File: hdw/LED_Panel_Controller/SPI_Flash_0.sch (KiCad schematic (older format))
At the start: 14 parts

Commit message: lots of schematic progress
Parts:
- removed U?: 74LVC1G07, TO_SOT_Packages_SMD:SOT-353_SC-70-5, symbol Custom_Library:74LVC1G07_Power
- added U?: 74LVC1G97, Package_TO_SOT_SMD:SOT-363_SC-70-6, symbol Custom_Library:74LVC1G97_Power_BUF
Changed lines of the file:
@@
 encoding utf-8
 Sheet 23 34
-Title "Electronic Display Logic Board"
-Date "2018-12-15"
+Title "LED Panel Controller"
+Date "2020-12-23"
 Rev "A"
-Comp "Marquette University Senior Design 2018/2019 Group E44"
+Comp "Drew Maatman, Logan Wedel"
 Comment1 ""
 Comment2 ""
@@
 F 7 "311-1344-1-ND" H 2435 7400 60  0001 C CNN "Digi-Key PN"
 	1    2010 6900
-	1    0    0    -1
-$EndComp
-$Comp
-L Custom_Library:74LVC1G07_Power U?
-U 1 1 5C161AE1
-P 1670 6320
-F 0 "U?" H 1770 6420 50  0000 L CNN
-F 1 "74LVC1G07" H 1770 6220 50  0000 L CNN
-F 2 "TO_SOT_Packages_SMD:SOT-353_SC-70-5" H 1670 6320 50  0001 C CNN
-F 3 "http://www.ti.com/lit/sg/scyt129e/scyt129e.pdf" H 1670 6320 50  0001 C CNN
-F 4 "296-8486-1-ND" H 1670 6320 50  0001 C CNN "Digi-Key PN"
-	1    1670 6320
 	1    0    0    -1
 $EndComp
@@
 	0    -1   1    0
 $EndComp
+$Comp
+L Custom_Library:74LVC1G97_Power_BUF U?
+U 1 1 5FE9D8D5
+P 1670 6320
+F 0 "U?" H 1730 6470 50  0000 L CNN
+F 1 "74LVC1G97" H 1730 6170 50  0000 L CNN
+F 2 "Package_TO_SOT_SMD:SOT-363_SC-70-6" H 1720 6320 50  0001 C CNN
+F 3 "http://www.ti.com/lit/ds/symlink/sn74lvc1g97.pdf" H 1720 6320 50  0001 C CNN
+	1    1670 6320
+	1    0    0    -1
+$EndComp
 $EndSCHEMATC

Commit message: made a lot more schematic progress
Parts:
- removed C?: 0.1uF, Capacitors_SMD:C_0603, symbol Custom_Library:C_Custom
- removed R? (x2): 10k, Resistors_SMD:R_0603, symbol Custom_Library:R_Custom
- removed R?: 1k, Resistors_SMD:R_0603, symbol Custom_Library:R_Custom
- added C?: 0.1uF, Capacitors_SMD:C_0603, symbol Custom_Library:C_Custom
- added R? (x2): 10k, Resistors_SMD:R_0603, symbol Custom_Library:R_Custom
- added R?: 1k, Resistors_SMD:R_0603, symbol Custom_Library:R_Custom
- C?, D?, R? (x4), U? (x2): Configuration (none) -> SPI_FLASH
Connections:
- net +3V3: now also C?.1, R?.1, R?.1
- net GND: now also C?.2, R?.2
- net at R?.1, U?.5 (SI): now also R?.1
- net at R?.1, U?.1 (~CE): now also R?.2
- net at D?.2 (A): now also R?.2
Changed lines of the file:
@@
-$Comp
-L Custom_Library:R_Custom R?
-U 1 1 5BB4E3FC
-P 5150 3930
-F 0 "R?" H 5090 3930 50  0000 R CNN
-F 1 "10k" V 5150 3930 50  0000 C CNN
-F 2 "Resistors_SMD:R_0603" H 5150 3930 50  0001 C CNN
-F 3 "" H 5150 3930 50  0001 C CNN
-F 4 "0603" H 5230 4010 50  0000 L CNN "display_footprint"
-F 5 "1%" H 5230 3930 50  0000 L CNN "Tolerance"
-F 6 "1/10W" H 5230 3850 50  0000 L CNN "Wattage"
-F 7 "RMCF0603FT10K0CT-ND" H 5450 4330 60  0001 C CNN "Digi-Key PN"
-	1    5150 3930
-	1    0    0    -1
-$EndComp
-$Comp
-L Custom_Library:R_Custom R?
-U 1 1 5BB4EBA3
-P 3930 3130
-F 0 "R?" H 3870 3130 50  0000 R CNN
-F 1 "10k" V 3930 3130 50  0000 C CNN
-F 2 "Resistors_SMD:R_0603" H 3930 3130 50  0001 C CNN
-F 3 "" H 3930 3130 50  0001 C CNN
-F 4 "0603" H 4010 3210 50  0000 L CNN "display_footprint"
-F 5 "1%" H 4010 3130 50  0000 L CNN "Tolerance"
-F 6 "1/10W" H 4010 3050 50  0000 L CNN "Wattage"
-F 7 "RMCF0603FT10K0CT-ND" H 4230 3530 60  0001 C CNN "Digi-Key PN"
-	1    3930 3130
-	1    0    0    -1
-$EndComp
 $Comp
 L Custom_Library:R_Custom R?
@@
 F 5 "1%" V 3620 3450 50  0001 C CNN "Tolerance"
 F 6 "1/16W" V 3720 3450 50  0001 C CNN "Wattage"
+F 7 "SPI_FLASH" V 3270 3450 50  0000 C CNN "Configuration"
 	1    3420 3450
 	0    1    1    0
@@
 F 6 "X7R" H 1860 6800 50  0000 R CNN "Dielectric"
 F 7 "311-1344-1-ND" H 2435 7400 60  0001 C CNN "Digi-Key PN"
+F 8 "SPI_FLASH" H 2340 6900 50  0000 C CNN "Configuration"
 	1    2010 6900
 	1    0    0    -1
@@
 	2410 6320 2410 6160
 $Comp
-L Custom_Library:R_Custom R?
-U 1 1 5C166A8D
-P 2410 5710
-AR Path="/5BAAE1F3/5C166A8D" Ref="R?"  Part="1"
-AR Path="/5BAAE1DC/5C166A8D" Ref="R?"  Part="1"
-AR Path="/5BAAE16C/5C166A8D" Ref="R?"  Part="1"
-AR Path="/5BB844FD/5C166A8D" Ref="R?"  Part="1"
-AR Path="/5BF346B3/5C166A8D" Ref="R?"  Part="1"
-AR Path="/5BB2595E/5C166A8D" Ref="R?"  Part="1"
-AR Path="/5F583577/5C166A8D" Ref="R?"  Part="1"
-F 0 "R?" H 2350 5710 50  0000 R CNN
-F 1 "1k" V 2410 5710 50  0000 C CNN
-F 2 "Resistors_SMD:R_0603" H 2410 5710 50  0001 C CNN
-F 3 "" H 2410 5710 50  0001 C CNN
-F 4 "0603" H 2480 5790 50  0000 L CNN "display_footprint"
-F 5 "1%" H 2480 5710 50  0000 L CNN "Tolerance"
-F 6 "1/10W" H 2480 5640 50  0000 L CNN "Wattage"
-F 7 "RMCF0603FT1K00CT-ND" H 2710 6110 60  0001 C CNN "Digi-Key PN"
-	1    2410 5710
-	-1   0    0    -1
-$EndComp
-$Comp
 L Device:LED D?
 U 1 1 5C166A95
@@
 AR Path="/5BB2595E/5C166A95" Ref="D?"  Part="1"
 AR Path="/5F583577/5C166A95" Ref="D?"  Part="1"
-F 0 "D?" V 2440 5890 50  0000 R CNN
-F 1 "Green" V 2357 5893 50  0000 R CNN
+F 0 "D?" V 2520 6120 50  0000 L CNN
+F 1 "Green" V 2420 6120 50  0000 L CNN
 F 2 "LEDs:LED_0603" H 2410 6010 50  0001 C CNN
 F 3 "~" H 2410 6010 50  0001 C CNN
 F 4 "160-1446-1-ND" H -2600 3010 50  0001 C CNN "Digi-Key PN"
+F 5 "SPI_FLASH" V 2320 6120 50  0000 L CNN "Configuration"
 	1    2410 6010
 	0    -1   -1   0
@@
 F 3 "http://ww1.microchip.com/downloads/en/DeviceDoc/20005045C.pdf" H 6030 4200 50  0001 C CNN
 F 4 "SST25VF080B-50-4I-S2AF-TCT-ND" H 6080 3650 50  0001 C CNN "Digi-Key PN"
+F 5 "SPI_FLASH" H 6080 3020 50  0000 C CNN "Configuration"
 	1    6080 3650
-	1    0    0    -1
-$EndComp
-$Comp
-L Custom_Library:C_Custom C?
-U 1 1 5F68928C
-P 6210 4700
-AR Path="/5BAAE16C/5F68928C" Ref="C?"  Part="1"
-AR Path="/5BB181D8/5F68928C" Ref="C?"  Part="1"
-AR Path="/5BB2595E/5F68928C" Ref="C?"  Part="1"
-AR Path="/5F583577/5F68928C" Ref="C?"  Part="1"
-F 0 "C?" H 6235 4800 50  0000 L CNN
-F 1 "0.1uF" H 6235 4600 50  0000 L CNN
-F 2 "Capacitors_SMD:C_0603" H 6248 4550 50  0001 C CNN
-F 3 "" H 6235 4800 50  0001 C CNN
-F 4 "0603" H 6060 4800 50  0000 R CNN "display_footprint"
-F 5 "50V" H 6060 4700 50  0000 R CNN "Voltage"
-F 6 "X7R" H 6060 4600 50  0000 R CNN "Dielectric"
-F 7 "311-1344-1-ND" H 6635 5200 60  0001 C CNN "Digi-Key PN"
-	1    6210 4700
 	1    0    0    -1
 $EndComp
@@
 F 6 "1/10W" H 4580 3850 50  0000 L CNN "Wattage"
 F 7 "RMCF0603FT10K0CT-ND" H 4800 4330 60  0001 C CNN "Digi-Key PN"
+F 8 "SPI_FLASH" H 4580 3770 50  0000 L CNN "Configuration"
 	1    4500 3930
 	1    0    0    -1
@@
 F 5 "1%" V 3620 3550 50  0001 C CNN "Tolerance"
 F 6 "1/16W" V 3720 3550 50  0001 C CNN "Wattage"
+F 7 "SPI_FLASH" H 3420 3550 50  0001 C CNN "Configuration"
 	1    3420 3550
 	0    1    1    0
@@
 F 5 "1%" V 3620 3650 50  0001 C CNN "Tolerance"
 F 6 "1/16W" V 3720 3650 50  0001 C CNN "Wattage"
+F 7 "SPI_FLASH" H 3420 3650 50  0001 C CNN "Configuration"
 	1    3420 3650
 	0    1    1    0
@@
 F 2 "Package_TO_SOT_SMD:SOT-363_SC-70-6" H 1720 6320 50  0001 C CNN
 F 3 "http://www.ti.com/lit/ds/symlink/sn74lvc1g97.pdf" H 1720 6320 50  0001 C CNN
+F 4 "SPI_FLASH" H 1370 6470 50  0000 C CNN "Configuration"
 	1    1670 6320
 	1    0    0    -1
 $EndComp
+$Comp
+L Custom_Library:R_Custom R?
+U 1 1 6026393A
+P 5150 3930
+F 0 "R?" H 5090 3930 50  0000 R CNN
+F 1 "10k" V 5150 3930 50  0000 C CNN
+F 2 "Resistors_SMD:R_0603" H 5150 3930 50  0001 C CNN
+F 3 "" H 5150 3930 50  0001 C CNN
+F 4 "0603" H 5230 4010 50  0000 L CNN "display_footprint"
+F 5 "1%" H 5230 3930 50  0000 L CNN "Tolerance"
+F 6 "1/10W" H 5230 3850 50  0000 L CNN "Wattage"
+F 7 "RMCF0603FT10K0CT-ND" H 5450 4330 60  0001 C CNN "Digi-Key PN"
+F 8 "SPI_FLASH" H 5230 3770 50  0000 L CNN "Configuration"
+	1    5150 3930
+	1    0    0    -1
+$EndComp
+$Comp
+L Custom_Library:R_Custom R?
+U 1 1 60263FB7
+P 3930 3130
+F 0 "R?" H 3870 3130 50  0000 R CNN
+F 1 "10k" V 3930 3130 50  0000 C CNN
+F 2 "Resistors_SMD:R_0603" H 3930 3130 50  0001 C CNN
+F 3 "" H 3930 3130 50  0001 C CNN
+F 4 "0603" H 4010 3210 50  0000 L CNN "display_footprint"
+F 5 "1%" H 4010 3130 50  0000 L CNN "Tolerance"
+F 6 "1/10W" H 4010 3050 50  0000 L CNN "Wattage"
+F 7 "RMCF0603FT10K0CT-ND" H 4230 3530 60  0001 C CNN "Digi-Key PN"
+F 8 "SPI_FLASH" H 4010 2970 50  0000 L CNN "Configuration"
+	1    3930 3130
+	1    0    0    -1
+$EndComp
+$Comp
+L Custom_Library:R_Custom R?
+U 1 1 60266213
+P 2410 5710
+F 0 "R?" H 2350 5710 50  0000 R CNN
+F 1 "1k" V 2410 5710 50  0000 C CNN
+F 2 "Resistors_SMD:R_0603" H 2410 5710 50  0001 C CNN
+F 3 "" H 2410 5710 50  0001 C CNN
+F 4 "0603" H 2490 5790 50  0000 L CNN "display_footprint"
+F 5 "1%" H 2490 5710 50  0000 L CNN "Tolerance"
+F 6 "1/10W" H 2490 5630 50  0000 L CNN "Wattage"
+F 7 "RMCF0603FT10K0CT-ND" H 2710 6110 60  0001 C CNN "Digi-Key PN"
+F 8 "SPI_FLASH" H 2490 5550 50  0000 L CNN "Configuration"
+	1    2410 5710
+	1    0    0    -1
+$EndComp
+$Comp
+L Custom_Library:C_Custom C?
+U 1 1 60269564
+P 6210 4700
+AR Path="/5BAAE16C/60269564" Ref="C?"  Part="1"
+AR Path="/5BB181D8/60269564" Ref="C?"  Part="1"
+AR Path="/5BB2595E/60269564" Ref="C?"  Part="1"
+AR Path="/5F583577/60269564" Ref="C?"  Part="1"
+F 0 "C?" H 6235 4800 50  0000 L CNN
+F 1 "0.1uF" H 6235 4600 50  0000 L CNN
+F 2 "Capacitors_SMD:C_0603" H 6248 4550 50  0001 C CNN
+F 3 "" H 6235 4800 50  0001 C CNN
+F 4 "0603" H 6060 4800 50  0000 R CNN "display_footprint"
+F 5 "50V" H 6060 4700 50  0000 R CNN "Voltage"
+F 6 "X7R" H 6060 4600 50  0000 R CNN "Dielectric"
+F 7 "311-1344-1-ND" H 6635 5200 60  0001 C CNN "Digi-Key PN"
+F 8 "SPI_FLASH" H 6540 4700 50  0000 C CNN "Configuration"
+	1    6210 4700
+	1    0    0    -1
+$EndComp

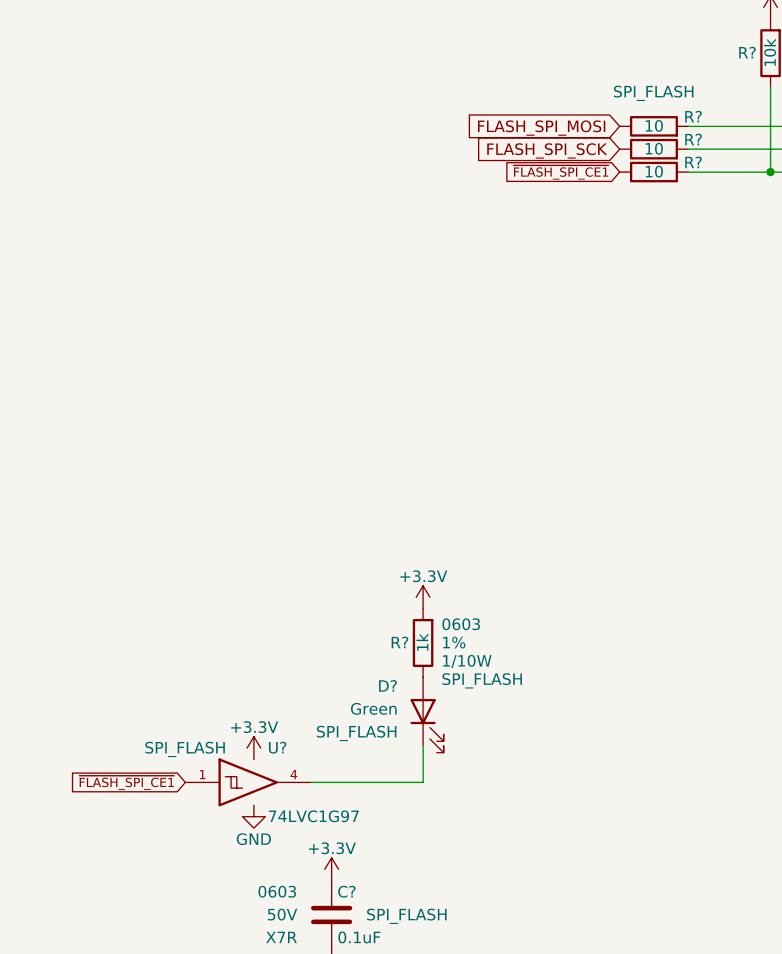
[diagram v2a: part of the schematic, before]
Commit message: lots of MCU pin assignments
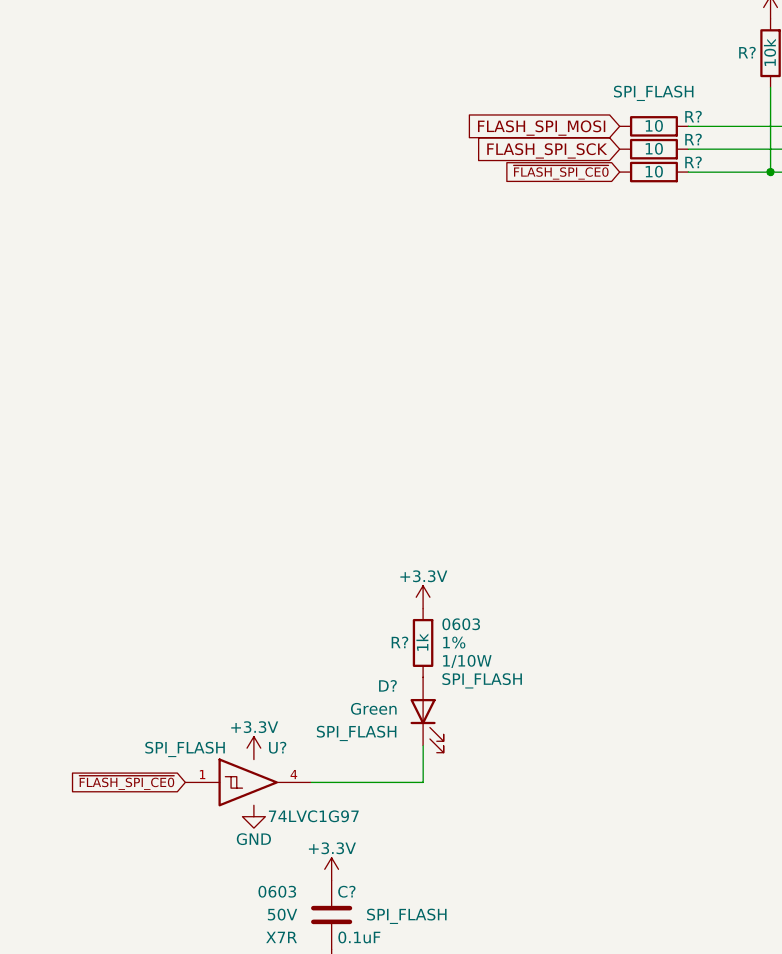
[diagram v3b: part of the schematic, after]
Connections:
- net ~FLASH_SPI_CE1 renamed ~FLASH_SPI_CE0
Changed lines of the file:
@@
 FLASH_SPI_SCK
 Text GLabel 3270 3650 0    40   Input ~ 0
-~FLASH_SPI_CE1
+~FLASH_SPI_CE0
 Text GLabel 3270 3450 0    50   Input ~ 0
 FLASH_SPI_MOSI
@@
 $EndComp
 Text GLabel 1370 6320 0    40   Input ~ 0
-~FLASH_SPI_CE1
+~FLASH_SPI_CE0
 $Comp
 L power:+3.3V #PWR?
